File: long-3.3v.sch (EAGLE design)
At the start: 31 parts, among them U1 USD-SOCKET, U2 MCP73831, U4 ADXL375BCCZ, X1 Micro USB, X2 CRYSTALS-NOGND-12SMX-B

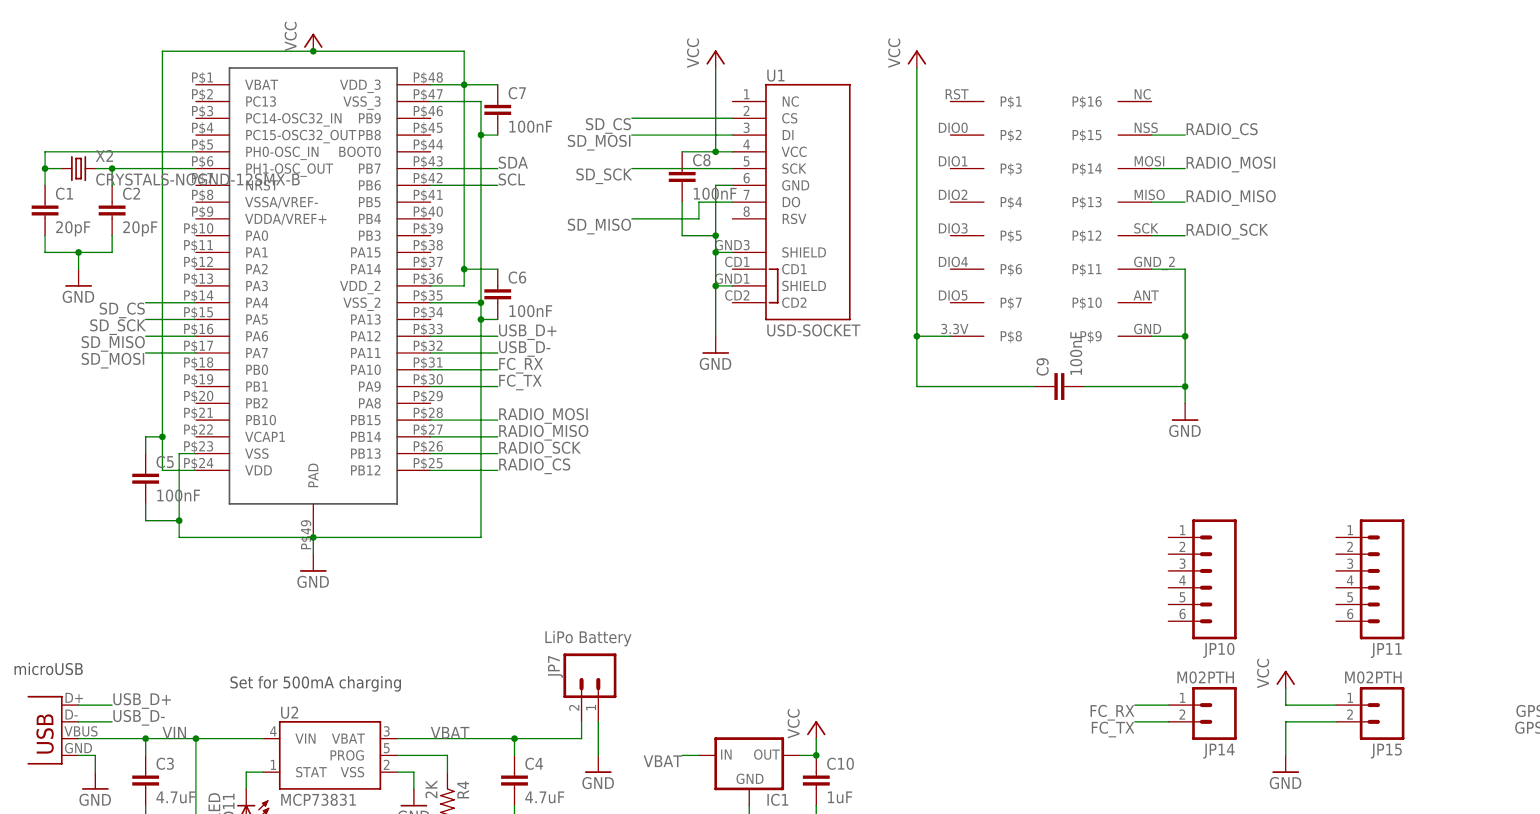
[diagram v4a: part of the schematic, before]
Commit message: Added more parts, routed more lines Added UFL connector (unrouted) Added and routed pullups, programming header, and other stuff
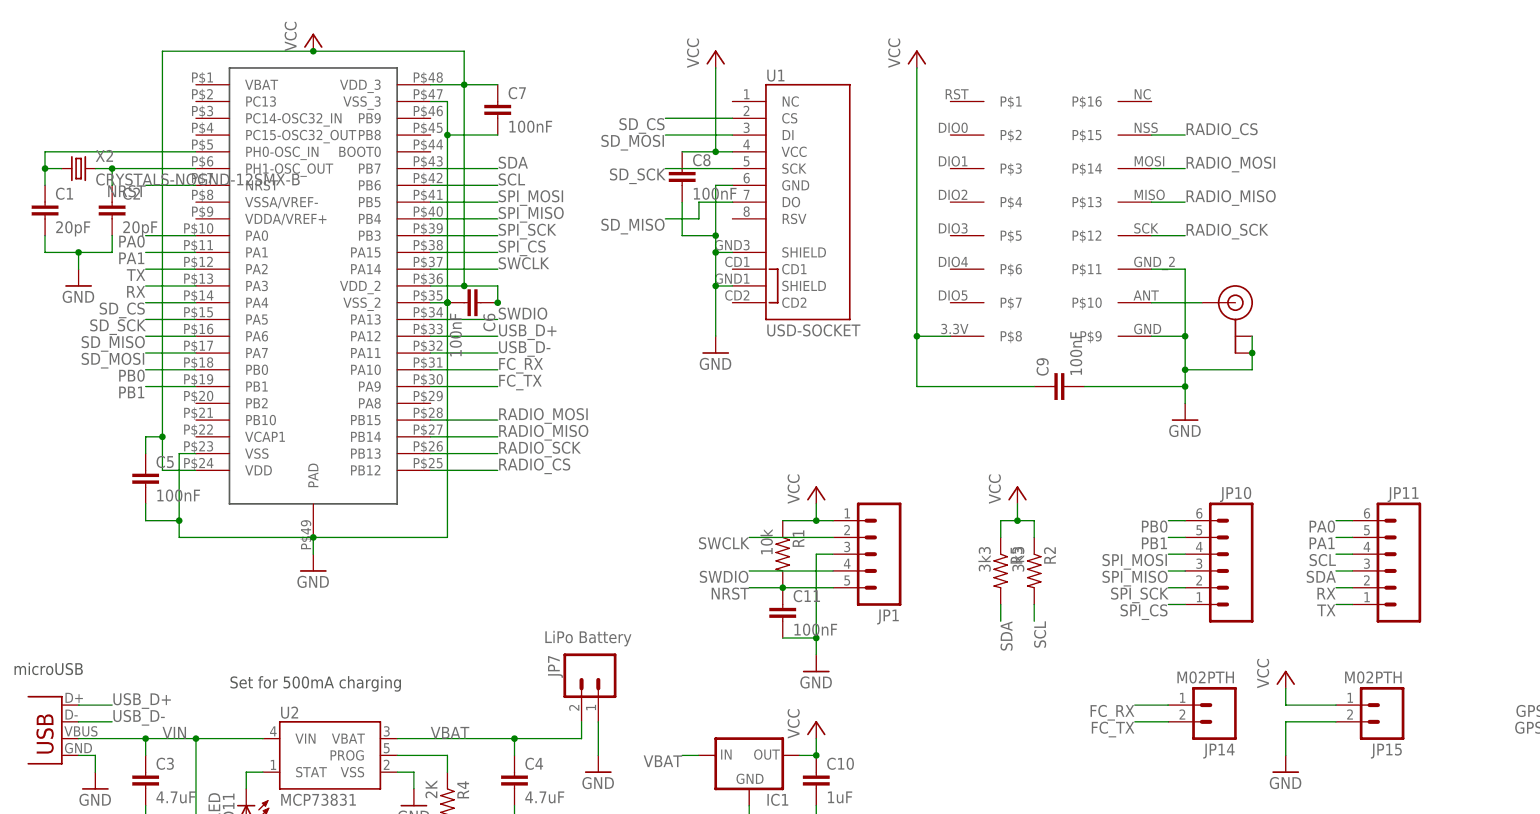
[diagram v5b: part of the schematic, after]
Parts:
- added C11: 100nF, rcl:C-EUC0402
- added JP1: (no value), SparkFun:M05PTH
- added R1: 10k, SparkFun:RESISTOR0402-RES
- added R2, R5: 3k3, SparkFun:RESISTOR0402-RES
- added U$4: U.FL, SparkFun:U.FL
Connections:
- new net N$4: U$3.P$10, U$4.SIGNAL
- new net NRST: C11.1, JP1.5, R1.2, U$1.NRST
- new net PA0: JP11.6, U$1.PA0
- new net PA1: JP11.5, U$1.PA1
- new net PB0: JP10.6, U$1.PB0
- new net PB1: JP10.5, U$1.PB1
- new net RX: JP11.2, U$1.PA3
- new net SPI_CS: JP10.1, U$1.PA15
- new net SPI_MISO: JP10.3, U$1.PB4
- new net SPI_MOSI: JP10.4, U$1.PB5
- new net SPI_SCK: JP10.2, U$1.PB3
- new net SWCLK: JP1.2, U$1.PA14
- new net SWDIO: JP1.4, U$1.PA13
- new net TX: JP11.1, U$1.PA2
- net GND: now also C11.2, JP1.3, U$4.GND@0, U$4.GND@1
- net SCL: now also JP11.4, R2.2
- net SDA: now also JP11.3, R5.2
- net VCC: now also JP1.1, R1.1, R2.1, R5.1
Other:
- moved on the sheet: C6, JP10, JP11

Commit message: fixed headers
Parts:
- X2: value CRYSTALS-NOGND-12SMX-B -> CRYSTAL
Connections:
- net FC_RX: now also JP16.1; no longer JP14.1
- net FC_TX: now also JP16.2; no longer JP14.2
- net GPS_RX: now also JP14.2; no longer JP16.2
- net GPS_TX: now also JP14.1; no longer JP16.1
- net PA0: now also JP12.6
- net PA1: now also JP12.5
- net PB0: now also JP13.6
- net PB1: now also JP13.5
- net RX: now also JP12.2
- net SCL: now also JP12.4
- net SDA: now also JP12.3
- net SPI_CS: now also JP13.1
- net SPI_MISO: now also JP13.3
- net SPI_MOSI: now also JP13.4
- net SPI_SCK: now also JP13.2
- net TX: now also JP12.1

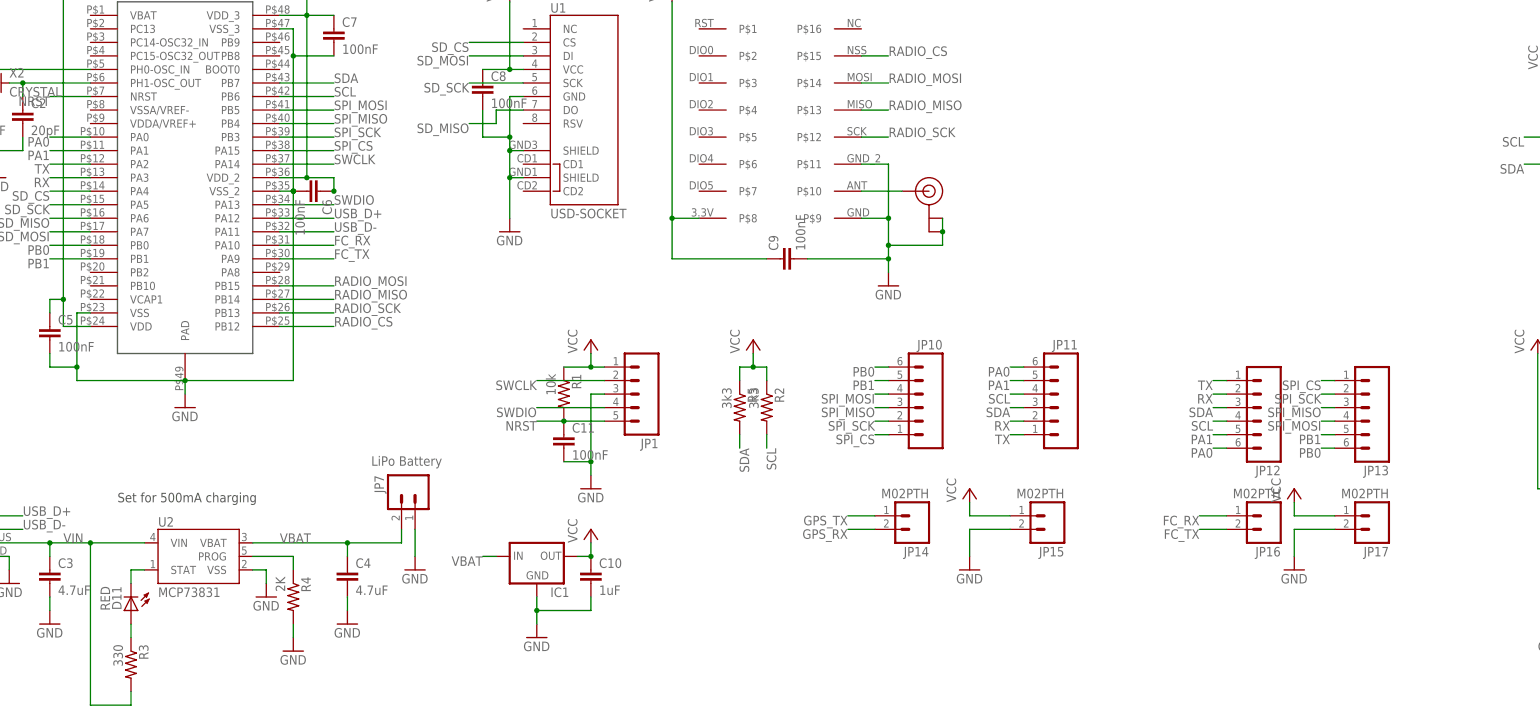
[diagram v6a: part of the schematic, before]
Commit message: fixed pins and added silk text
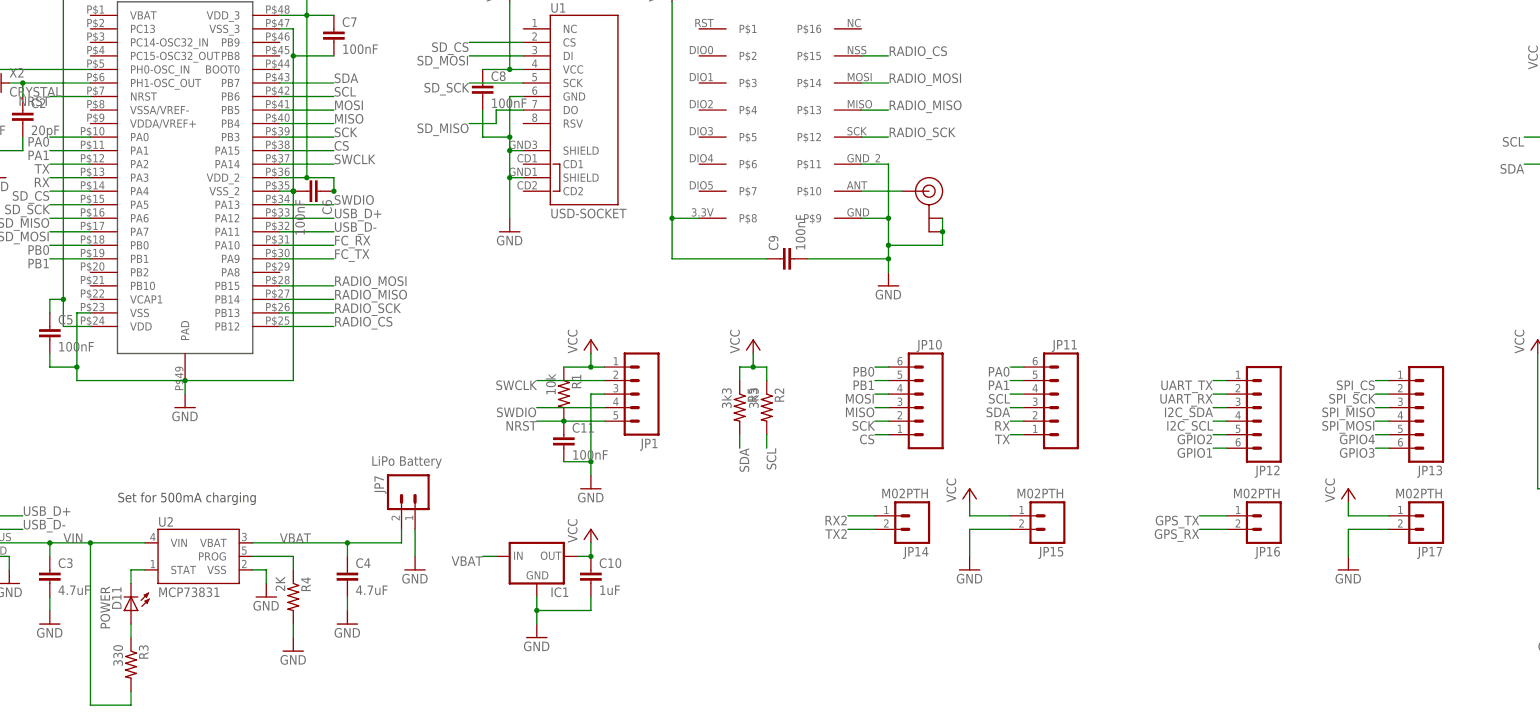
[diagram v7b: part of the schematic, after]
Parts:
- D11: value RED -> POWER
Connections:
- new net CS: JP10.1, U$1.PA15
- new net GPIO1: JP12.6
- new net GPIO2: JP12.5
- new net GPIO3: JP13.6
- new net GPIO4: JP13.5
- new net I2C_SCL: JP12.4
- new net I2C_SDA: JP12.3
- new net MISO: JP10.3, U$1.PB4
- new net MOSI: JP10.4, U$1.PB5
- new net RX2: JP14.1
- new net SCK: JP10.2, U$1.PB3
- new net TX2: JP14.2
- new net UART_RX: JP12.2
- new net UART_TX: JP12.1
- net FC_RX: no longer JP16.1
- net FC_TX: no longer JP16.2
- net GPS_RX: now also JP16.2; no longer JP14.2
- net GPS_TX: now also JP16.1; no longer JP14.1
- net PA0: no longer JP12.6
- net PA1: no longer JP12.5
- net PB0: no longer JP13.6
- net PB1: no longer JP13.5
- net RX: no longer JP12.2
- net SCL: no longer JP12.4
- net SDA: no longer JP12.3
- net SPI_CS: no longer JP10.1, U$1.PA15
- net SPI_MISO: no longer JP10.3, U$1.PB4
- net SPI_MOSI: no longer JP10.4, U$1.PB5
- net SPI_SCK: no longer JP10.2, U$1.PB3
- net TX: no longer JP12.1
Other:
- moved on the sheet: JP13, JP17

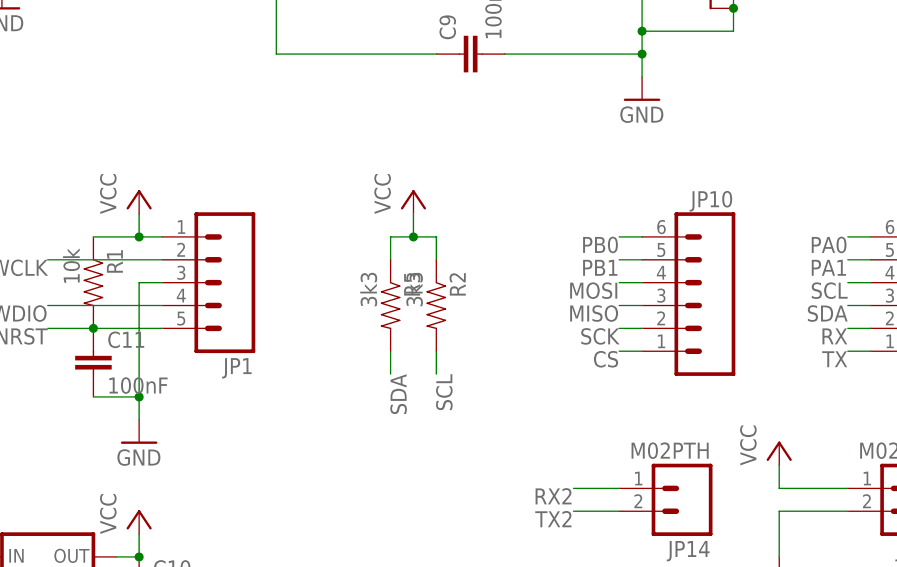
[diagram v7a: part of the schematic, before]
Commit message: Routed antenna in coplanar waveguide. Removed some other tracks to do it though. Matt's turn!
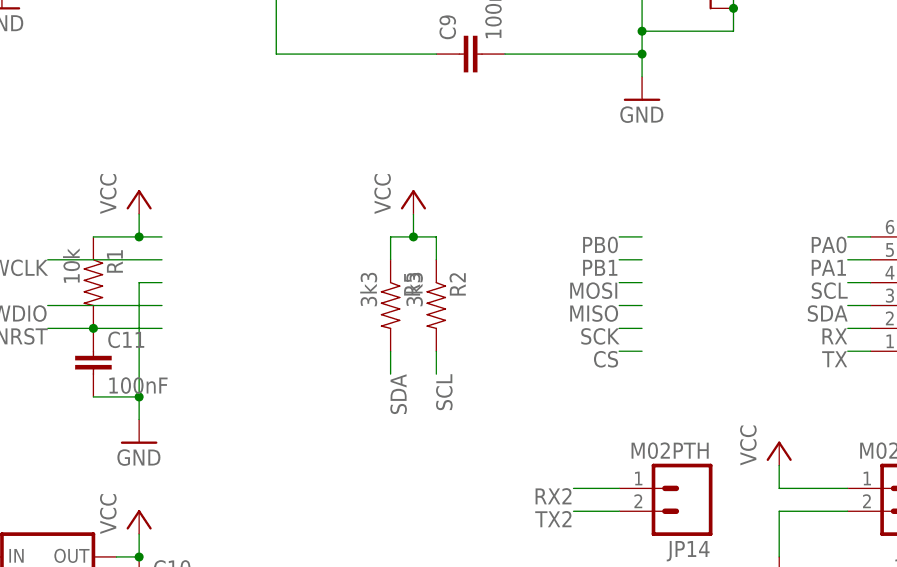
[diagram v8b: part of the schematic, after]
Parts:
- removed JP1: (no value), SparkFun:M05PTH
- removed JP10: (no value), SparkFun-Connectors:M06SIP
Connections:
- net CS: no longer JP10.1
- net GND: no longer JP1.3
- net MISO: no longer JP10.3
- net MOSI: no longer JP10.4
- net NRST: no longer JP1.5
- net PB0: no longer JP10.6
- net PB1: no longer JP10.5
- net SCK: no longer JP10.2
- net SWCLK: no longer JP1.2
- net SWDIO: no longer JP1.4
- net VCC: no longer JP1.1
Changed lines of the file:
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@@
 <?xml version="1.0" encoding="utf-8"?>
 <!DOCTYPE eagle SYSTEM "eagle.dtd">
-<eagle version="7.2.0">
+<eagle version="7.0.0">
 <drawing>
 <settings>
@@
 <part name="C9" library="rcl" deviceset="C-EU" device="C0402" value="100nF"/>
 <part name="C10" library="rcl" deviceset="C-EU" device="C0402" value="1uF"/>
-<part name="JP10" library="SparkFun-Connectors" deviceset="M06" device="SIP"/>
 <part name="JP11" library="SparkFun-Connectors" deviceset="M06" device="SIP"/>
 <part name="JP12" library="SparkFun-Connectors" deviceset="M06" device="SIP"/>
@@
 <part name="JP16" library="SparkFun-Connectors" deviceset="M02" device="PTH"/>
 <part name="JP17" library="SparkFun-Connectors" deviceset="M02" device="PTH"/>
-<part name="JP1" library="SparkFun" deviceset="M05" device="PTH"/>
 <part name="P+10" library="supply1" deviceset="VCC" device=""/>
 <part name="GND12" library="supply1" deviceset="GND" device=""/>
@@
 <instance part="C9" gate="G$1" x="165.1" y="93.98" rot="R90"/>
 <instance part="C10" gate="G$1" x="129.54" y="35.56"/>
-<instance part="JP10" gate="G$1" x="190.5" y="66.04" rot="MR0"/>
 <instance part="JP11" gate="G$1" x="215.9" y="66.04" rot="MR0"/>
 <instance part="JP12" gate="G$1" x="254" y="66.04" rot="R180"/>
@@
 <instance part="JP16" gate="G$1" x="256.54" y="45.72" rot="R180"/>
 <instance part="JP17" gate="G$1" x="287.02" y="45.72" rot="R180"/>
-<instance part="JP1" gate="G$1" x="139.7" y="68.58" rot="R180"/>
 <instance part="P+10" gate="VCC" x="129.54" y="78.74"/>
 <instance part="GND12" gate="1" x="129.54" y="50.8"/>
@@
 <segment>
 <pinref part="GND12" gate="1" pin="GND"/>
-<pinref part="JP1" gate="G$1" pin="3"/>
 <wire x1="132.08" y1="68.58" x2="129.54" y2="68.58" width="0.1524" layer="91"/>
 <wire x1="129.54" y1="68.58" x2="129.54" y2="55.88" width="0.1524" layer="91"/>
@@
 </segment>
 <segment>
-<pinref part="JP1" gate="G$1" pin="1"/>
 <wire x1="132.08" y1="73.66" x2="129.54" y2="73.66" width="0.1524" layer="91"/>
 <wire x1="129.54" y1="73.66" x2="129.54" y2="76.2" width="0.1524" layer="91"/>
@@
 </segment>
 <segment>
-<pinref part="JP1" gate="G$1" pin="4"/>
 <wire x1="132.08" y1="66.04" x2="119.38" y2="66.04" width="0.1524" layer="91"/>
 <label x="119.38" y="66.04" size="1.778" layer="95" rot="R180"/>
@@
 </segment>
 <segment>
-<pinref part="JP1" gate="G$1" pin="2"/>
 <wire x1="132.08" y1="71.12" x2="119.38" y2="71.12" width="0.1524" layer="91"/>
 <label x="119.38" y="71.12" size="1.778" layer="95" rot="R180"/>
@@
 <wire x1="185.42" y1="71.12" x2="182.88" y2="71.12" width="0.1524" layer="91"/>
 <label x="182.88" y="71.12" size="1.778" layer="95" rot="R180"/>
-<pinref part="JP10" gate="G$1" pin="5"/>
 </segment>
 <segment>
@@
 <wire x1="185.42" y1="73.66" x2="182.88" y2="73.66" width="0.1524" layer="91"/>
 <label x="182.88" y="73.66" size="1.778" layer="95" rot="R180"/>
-<pinref part="JP10" gate="G$1" pin="6"/>
 </segment>
 <segment>
@@
 <net name="NRST" class="0">
 <segment>
-<pinref part="JP1" gate="G$1" pin="5"/>
 <wire x1="132.08" y1="63.5" x2="124.46" y2="63.5" width="0.1524" layer="91"/>
 <label x="119.38" y="63.5" size="1.778" layer="95" rot="R180"/>
@@
 <wire x1="185.42" y1="60.96" x2="182.88" y2="60.96" width="0.1524" layer="91"/>
 <label x="182.88" y="60.96" size="1.778" layer="95" rot="R180"/>
-<pinref part="JP10" gate="G$1" pin="1"/>
 </segment>
 <segment>
@@
 <wire x1="185.42" y1="63.5" x2="182.88" y2="63.5" width="0.1524" layer="91"/>
 <label x="182.88" y="63.5" size="1.778" layer="95" rot="R180"/>
-<pinref part="JP10" gate="G$1" pin="2"/>
 </segment>
 <segment>
@@
 <wire x1="185.42" y1="66.04" x2="182.88" y2="66.04" width="0.1524" layer="91"/>
 <label x="182.88" y="66.04" size="1.778" layer="95" rot="R180"/>
-<pinref part="JP10" gate="G$1" pin="3"/>
 </segment>
 <segment>
@@
 <wire x1="185.42" y1="68.58" x2="182.88" y2="68.58" width="0.1524" layer="91"/>
 <label x="182.88" y="68.58" size="1.778" layer="95" rot="R180"/>
-<pinref part="JP10" gate="G$1" pin="4"/>
-</segment>
-<segment>
+</segment>
+<segment>
